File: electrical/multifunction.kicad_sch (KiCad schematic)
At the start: 16 parts

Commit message: Added smoke signal to GEA 24 and moved TOGA to GAD 27
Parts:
- added TOGA_SW: SW_Push, symbol Switch:SW_Push
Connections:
- net GND: now also CABIN_SW.2 (B), TOGA_SW.2
- net at GAD27.P271_9 (DISCRETE_IN_1): now also TOGA_SW.1
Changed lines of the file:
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@@
   (junction (at 160.02 123.19) (diameter 0) (color 0 0 0 0)
   )
+  (junction (at 160.02 120.65) (diameter 0) (color 0 0 0 0)
+  )
   (junction (at 110.49 213.36) (diameter 0) (color 0 0 0 0)
   )
@@
   )
   (junction (at 114.3 92.71) (diameter 0) (color 0 0 0 0)
+  )
+  (junction (at 114.3 72.39) (diameter 0) (color 0 0 0 0)
   )
   (junction (at 125.73 127) (diameter 0) (color 0 0 0 0)
@@
     (stroke (width 0) (type default))
   )
+  (wire (pts (xy 157.48 120.65) (xy 160.02 120.65))
+    (stroke (width 0) (type default))
+  )
   (wire (pts (xy 81.28 147.32) (xy 95.25 147.32))
     (stroke (width 0) (type default))
@@
     (stroke (width 0) (type default))
   )
+  (wire (pts (xy 97.79 44.45) (xy 114.3 44.45))
+    (stroke (width 0) (type default))
+  )
   (wire (pts (xy 81.28 217.17) (xy 124.46 217.17))
     (stroke (width 0) (type default))
@@
     (stroke (width 0) (type default))
   )
+  (wire (pts (xy 160.02 120.65) (xy 160.02 123.19))
+    (stroke (width 0) (type default))
+  )
   (wire (pts (xy 81.28 205.74) (xy 91.44 205.74))
     (stroke (width 0) (type default))
@@
     (stroke (width 0) (type default))
   )
+  (wire (pts (xy 81.28 44.45) (xy 87.63 44.45))
+    (stroke (width 0) (type default))
+  )
   (wire (pts (xy 114.3 74.93) (xy 114.3 72.39))
     (stroke (width 0) (type default))
@@
     (stroke (width 0) (type default))
   )
+  (wire (pts (xy 114.3 44.45) (xy 114.3 72.39))
+    (stroke (width 0) (type default))
+  )
   (wire (pts (xy 115.57 135.89) (xy 115.57 139.7))
     (stroke (width 0) (type default))
@@
     (stroke (width 0) (type default))
   )
-  (wire (pts (xy 160.02 118.11) (xy 160.02 123.19))
+  (wire (pts (xy 160.02 118.11) (xy 160.02 120.65))
     (stroke (width 0) (type default))
   )
@@
         )
       )
+    )
+  )
+  (symbol (lib_id "Switch:SW_Push") (at 92.71 44.45 0) (unit 1)
+    (in_bom yes) (on_board yes) (dnp no)
+    (property "Reference" "TOGA_SW" (at 121.92 44.45 0)
+      (effects (font (size 1.27 1.27)))
+    )
+    (property "Value" "SW_Push" (at 92.71 39.37 0)
+      (effects (font (size 1.27 1.27)) hide)
+    )
+    (property "Footprint" "" (at 92.71 39.37 0)
+      (effects (font (size 1.27 1.27)) hide)
+    )
+    (property "Datasheet" "~" (at 92.71 39.37 0)
+      (effects (font (size 1.27 1.27)) hide)
+    )
+    (pin "1")
+    (pin "2")
+    (instances
+      (project "electrical"
+        (path "/e8ec215a-dbe2-4eba-a577-e50a0a128049/67540fe5-9b6d-4d8c-9d03-cde1487f48ae"
+          (reference "TOGA_SW") (unit 1)
+        )
+      )

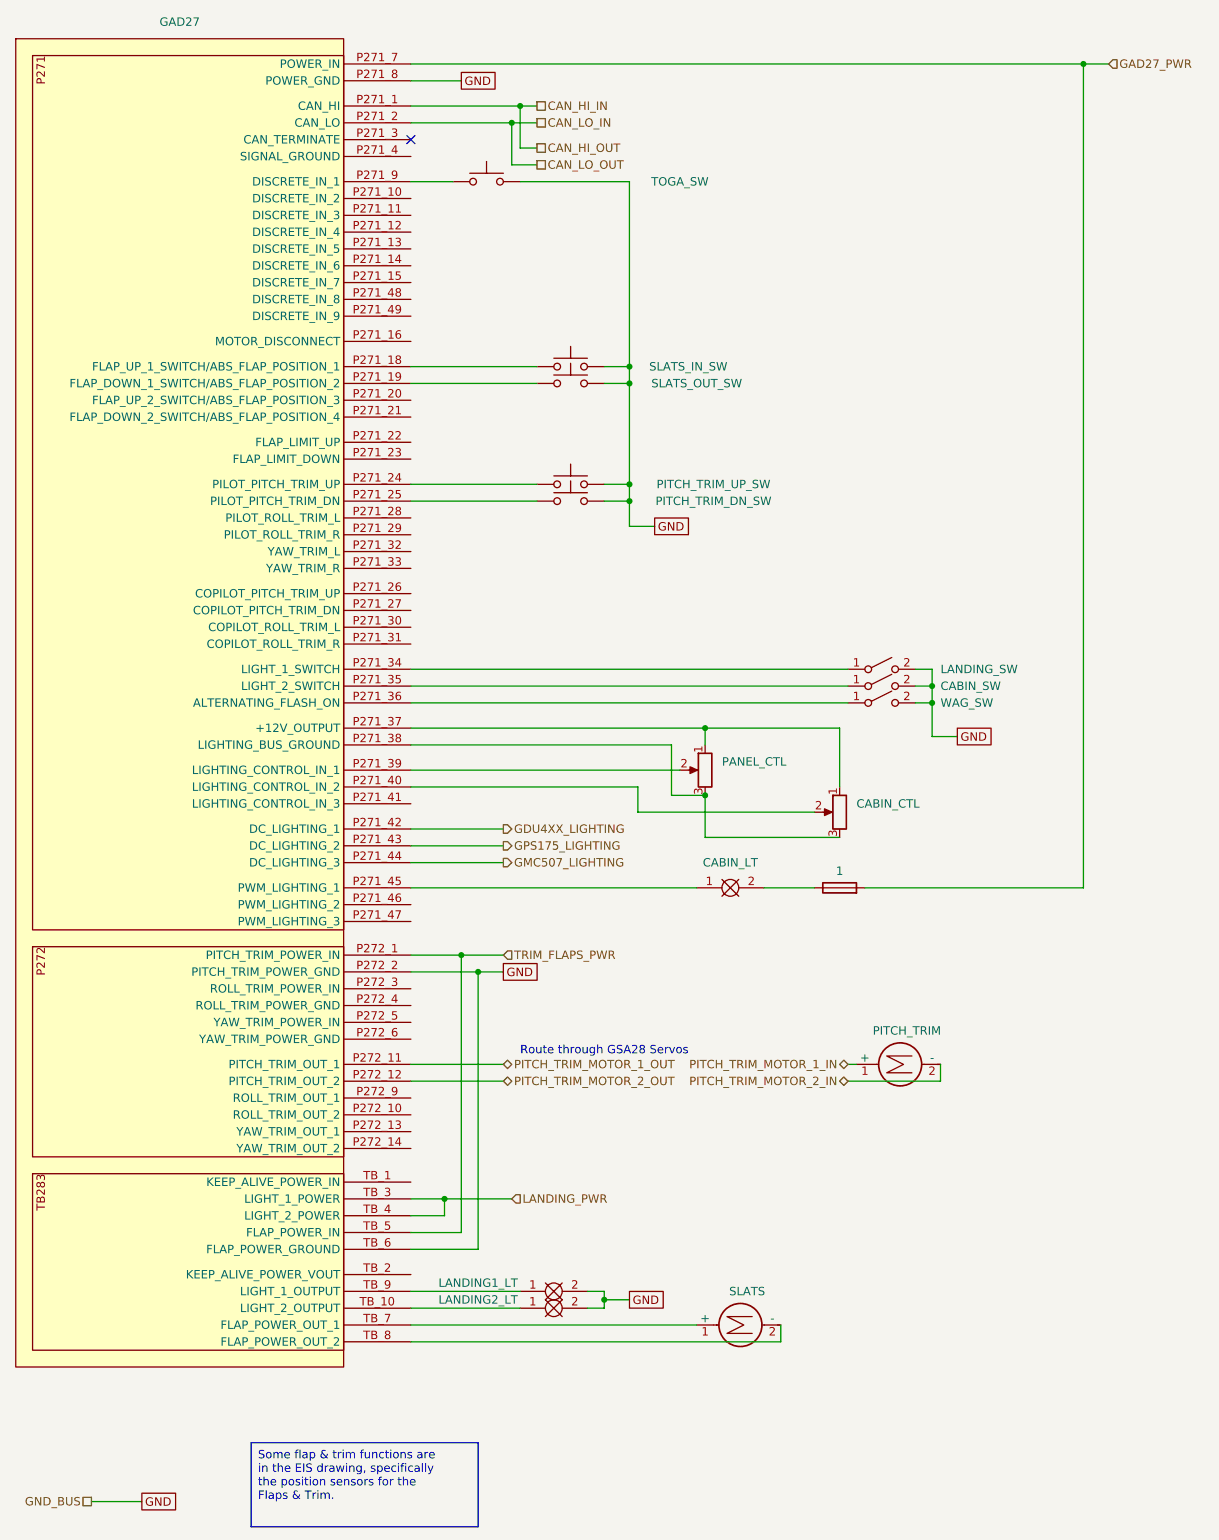
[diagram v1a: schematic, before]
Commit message: Changed grounds and canbuses to be in/out when applicable.
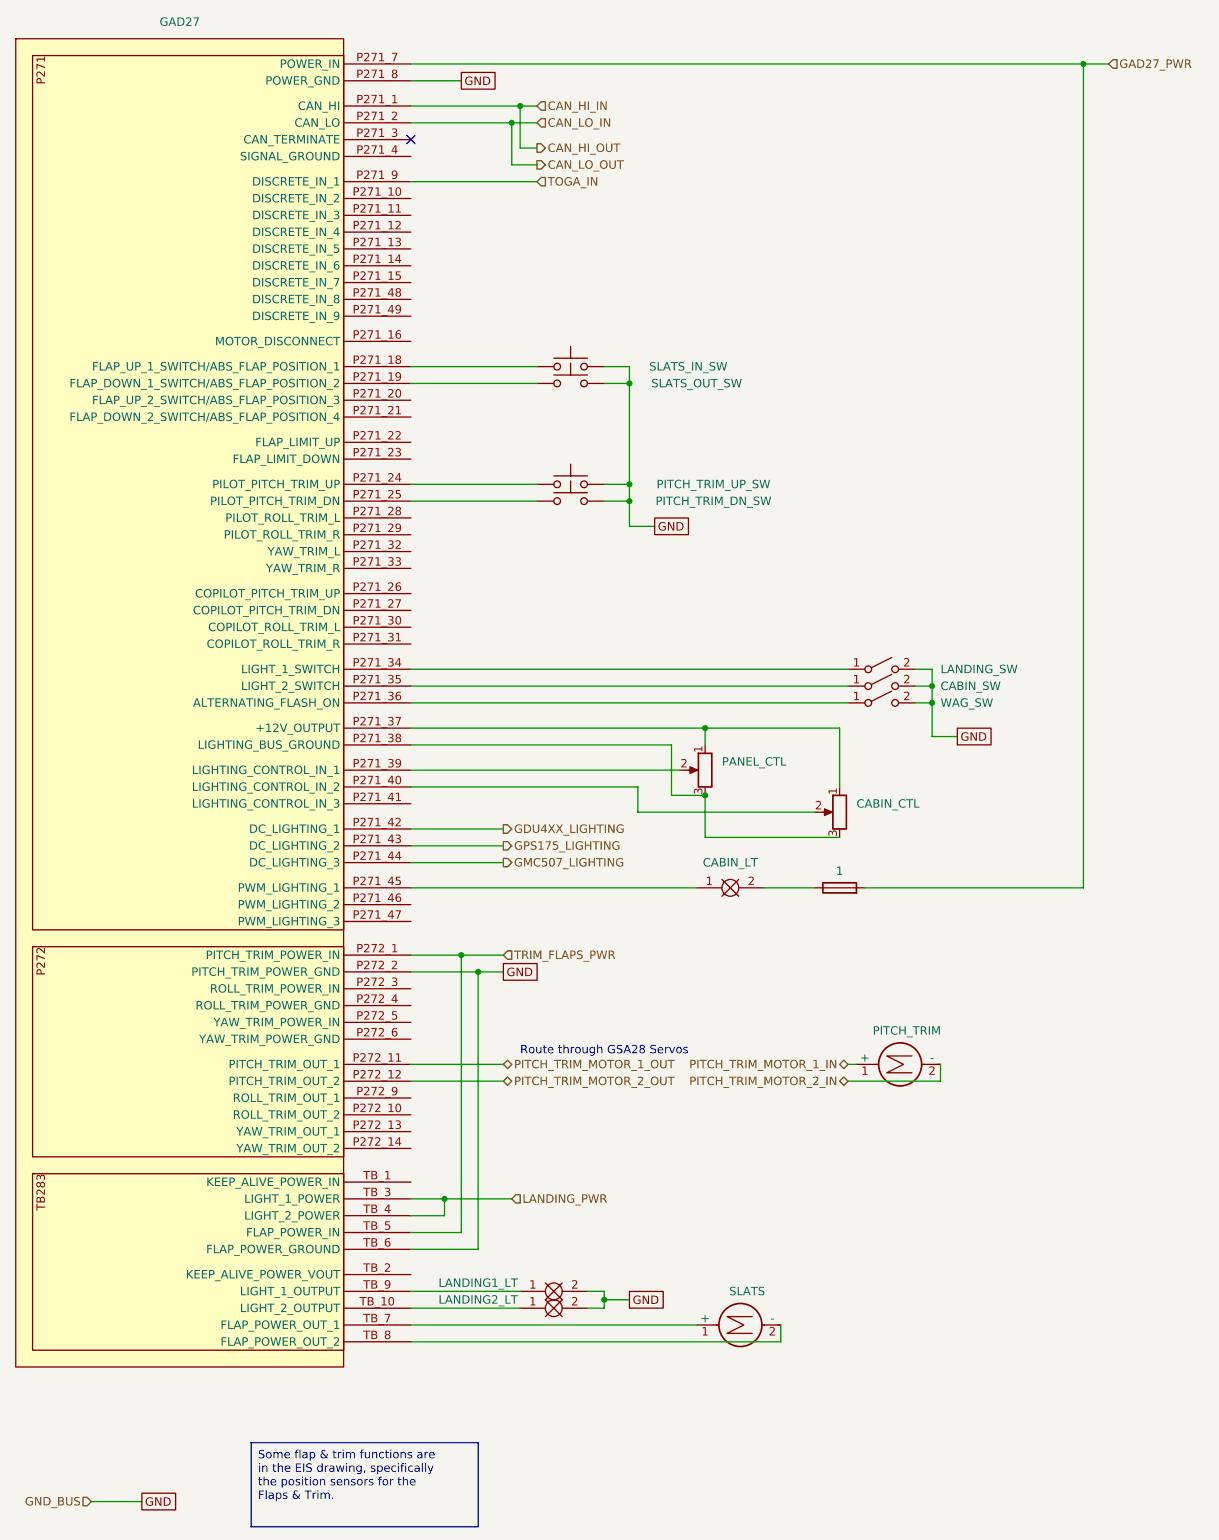
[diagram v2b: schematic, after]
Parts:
- removed TOGA_SW: SW_Push, symbol Switch:SW_Push
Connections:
- net TOGA_IN: now reaches GAD27.P271_9 (DISCRETE_IN_1)
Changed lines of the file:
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@@
   (junction (at 114.3 92.71) (diameter 0) (color 0 0 0 0)
-  )
-  (junction (at 114.3 72.39) (diameter 0) (color 0 0 0 0)
   )
   (junction (at 125.73 127) (diameter 0) (color 0 0 0 0)
@@
     (stroke (width 0) (type default))
   )
-  (wire (pts (xy 97.79 44.45) (xy 114.3 44.45))
-    (stroke (width 0) (type default))
-  )
   (wire (pts (xy 81.28 217.17) (xy 124.46 217.17))
     (stroke (width 0) (type default))
@@
     (stroke (width 0) (type default))
   )
-  (wire (pts (xy 81.28 44.45) (xy 87.63 44.45))
-    (stroke (width 0) (type default))
-  )
   (wire (pts (xy 114.3 74.93) (xy 114.3 72.39))
     (stroke (width 0) (type default))
@@
     (stroke (width 0) (type default))
   )
-  (wire (pts (xy 114.3 44.45) (xy 114.3 72.39))
-    (stroke (width 0) (type default))
-  )
   (wire (pts (xy 115.57 135.89) (xy 115.57 139.7))
+    (stroke (width 0) (type default))
+  )
+  (wire (pts (xy 81.28 44.45) (xy 100.33 44.45))
     (stroke (width 0) (type default))
   )
@@
     )
   )
-  (hierarchical_label "CAN_HI_IN" (shape passive) (at 100.33 33.02 0) (fields_autoplaced)
-    (effects (font (size 1.27 1.27)) (justify left))
-  )
-  (hierarchical_label "CAN_LO_IN" (shape passive) (at 100.33 35.56 0) (fields_autoplaced)
+  (hierarchical_label "CAN_HI_IN" (shape input) (at 100.33 33.02 0) (fields_autoplaced)
+    (effects (font (size 1.27 1.27)) (justify left))
+  )
+  (hierarchical_label "CAN_LO_IN" (shape input) (at 100.33 35.56 0) (fields_autoplaced)
+    (effects (font (size 1.27 1.27)) (justify left))
+  )
+  (hierarchical_label "TOGA_IN" (shape input) (at 100.33 44.45 0) (fields_autoplaced)
     (effects (font (size 1.27 1.27)) (justify left))
   )
@@
     (effects (font (size 1.27 1.27)) (justify left))
   )
-  (hierarchical_label "CAN_HI_OUT" (shape passive) (at 100.33 39.37 0) (fields_autoplaced)
+  (hierarchical_label "CAN_HI_OUT" (shape output) (at 100.33 39.37 0) (fields_autoplaced)
     (effects (font (size 1.27 1.27)) (justify left))
   )
@@
     (effects (font (size 1.27 1.27)) (justify left))
   )
-  (hierarchical_label "GND_BUS" (shape passive) (at 33.02 243.84 180) (fields_autoplaced)
+  (hierarchical_label "GND_BUS" (shape input) (at 33.02 243.84 180) (fields_autoplaced)
     (effects (font (size 1.27 1.27)) (justify right))
   )
@@
     (effects (font (size 1.27 1.27)) (justify right))
   )
-  (hierarchical_label "CAN_LO_OUT" (shape passive) (at 100.33 41.91 0) (fields_autoplaced)
+  (hierarchical_label "CAN_LO_OUT" (shape output) (at 100.33 41.91 0) (fields_autoplaced)
     (effects (font (size 1.27 1.27)) (justify left))
   )
@@
         )
       )
-    )
-  )
-  (symbol (lib_id "Switch:SW_Push") (at 92.71 44.45 0) (unit 1)
-    (in_bom yes) (on_board yes) (dnp no)
-    (property "Reference" "TOGA_SW" (at 121.92 44.45 0)
-      (effects (font (size 1.27 1.27)))
-    )
-    (property "Value" "SW_Push" (at 92.71 39.37 0)
-      (effects (font (size 1.27 1.27)) hide)
-    )
-    (property "Footprint" "" (at 92.71 39.37 0)
-      (effects (font (size 1.27 1.27)) hide)
-    )
-    (property "Datasheet" "~" (at 92.71 39.37 0)
-      (effects (font (size 1.27 1.27)) hide)
-    )
-    (pin "1")
-    (pin "2")
-    (instances
-      (project "electrical"
-        (path "/e8ec215a-dbe2-4eba-a577-e50a0a128049/67540fe5-9b6d-4d8c-9d03-cde1487f48ae"
-          (reference "TOGA_SW") (unit 1)
-        )
-      )

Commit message: Removed GAD 27 and just use VP-X. Not worth it for lights control and better wig-wag. VP-X is good enough and frees up breakers.
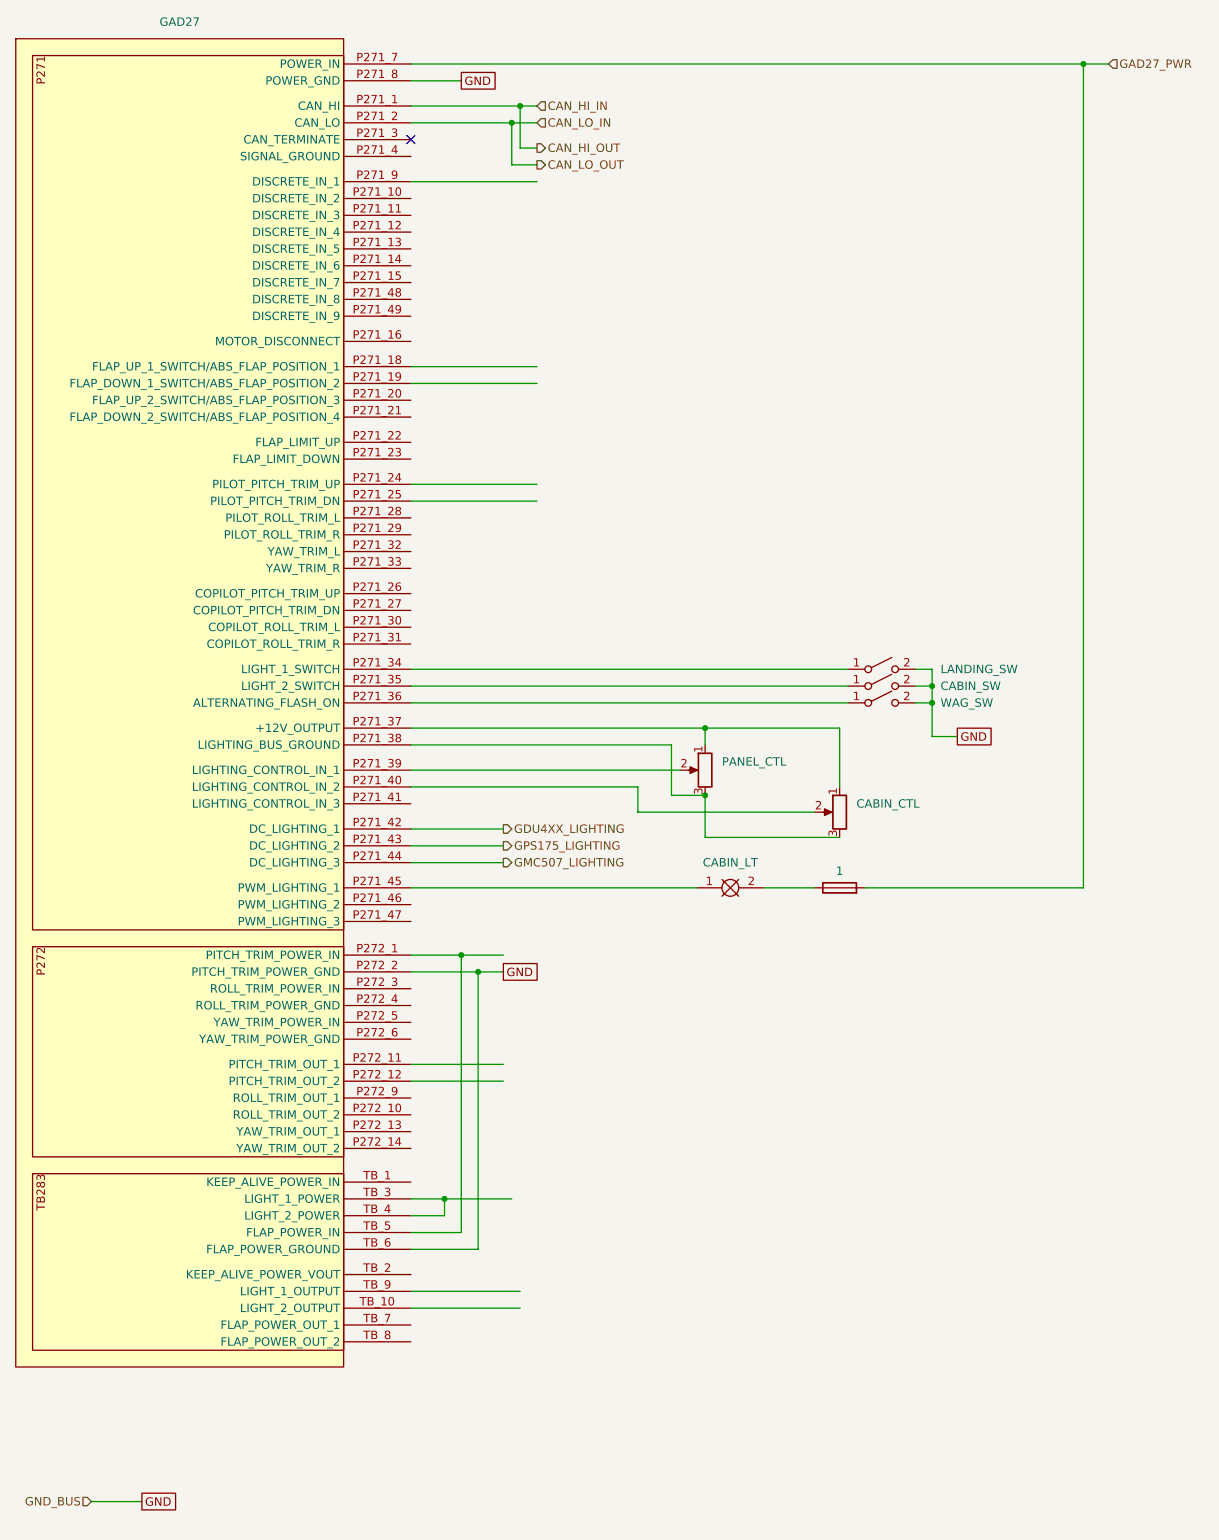
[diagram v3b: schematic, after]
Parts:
- removed LANDING1_LT, LANDING2_LT: ~, symbol flyerx:Bulb
- removed PITCH_TRIM, SLATS: Motor_DC, symbol Motor:Motor_DC
- removed PITCH_TRIM_DN_SW, PITCH_TRIM_UP_SW, SLATS_IN_SW, SLATS_OUT_SW: SW_Push, symbol Switch:SW_Push
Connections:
- net LANDING_PWR: no longer names the net of GAD27.TB_3 (LIGHT_1_POWER), GAD27.TB_4 (LIGHT_2_POWER)
- net PITCH_TRIM_MOTOR_1_OUT: no longer names the net of GAD27.P272_11 (PITCH_TRIM_OUT_1)
- net PITCH_TRIM_MOTOR_2_OUT: no longer names the net of GAD27.P272_12 (PITCH_TRIM_OUT_2)
- net TOGA_IN: no longer names the net of GAD27.P271_9 (DISCRETE_IN_1)
- net TRIM_FLAPS_PWR: no longer names the net of GAD27.P272_1 (PITCH_TRIM_POWER_IN), GAD27.TB_5 (FLAP_POWER_IN)
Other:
- note removed: "Route through GSA28 Servos"
